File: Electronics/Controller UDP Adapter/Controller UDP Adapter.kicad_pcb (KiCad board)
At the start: 2 copper layers, 99.5 x 101 mm, 23 parts, among them J1 GNSS, J2 Pulse_J0011D01BNL, J3 Pulse_J0011D01BNL

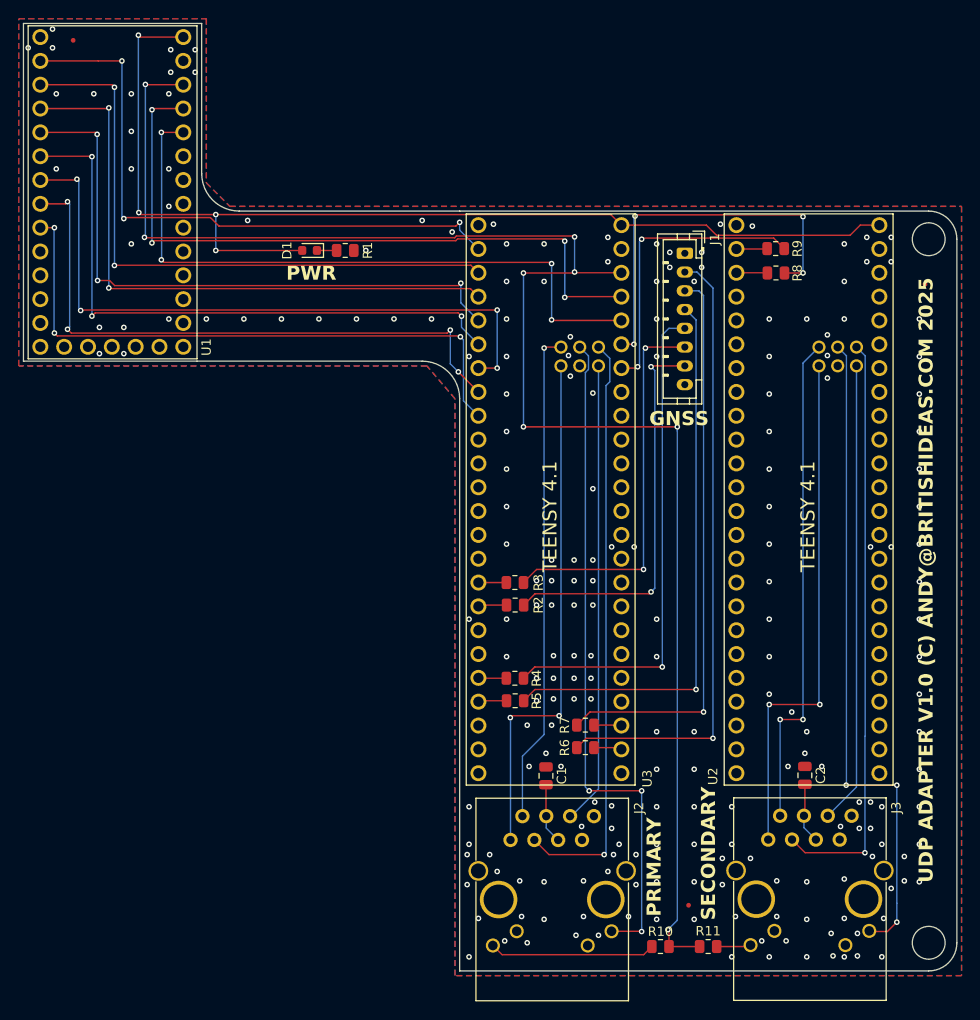
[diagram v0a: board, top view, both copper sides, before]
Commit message: Refactor, cleanup, changed PGN value size to 64 bits. Updates to base station.
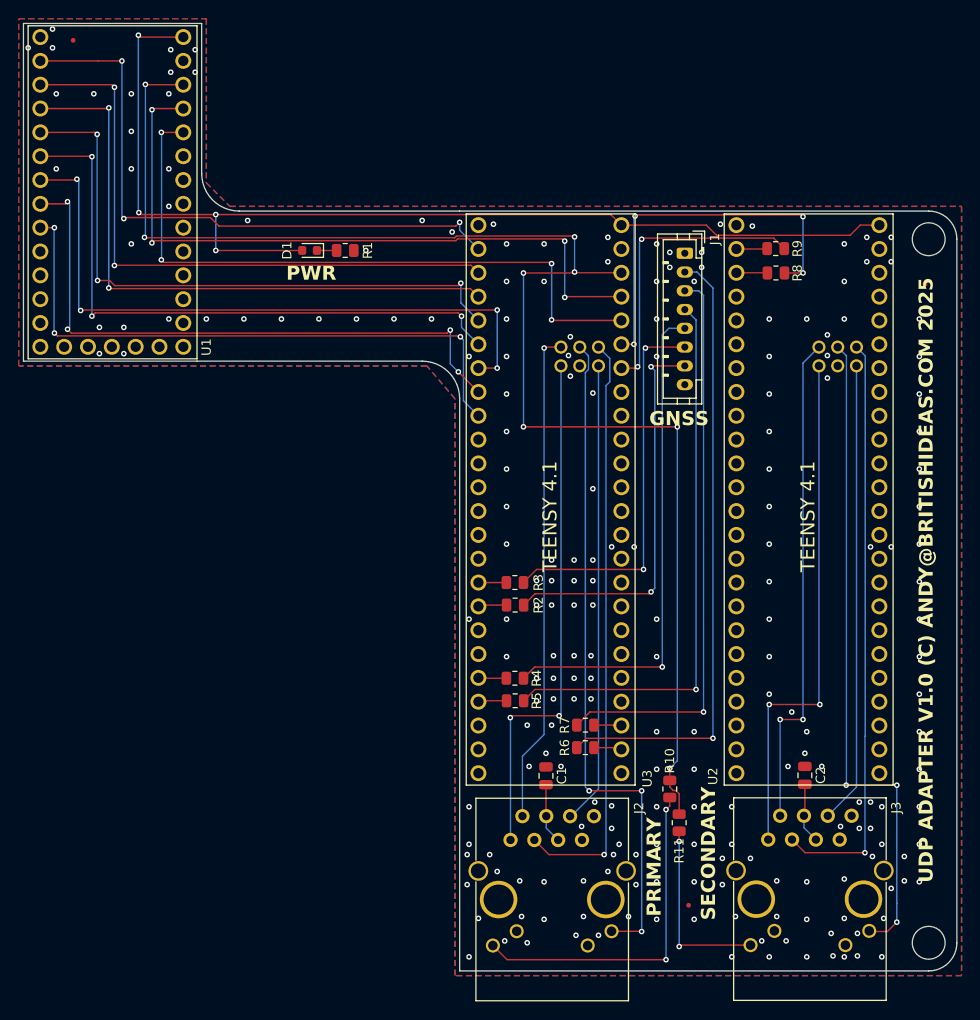
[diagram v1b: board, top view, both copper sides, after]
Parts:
- moved R10 16.8 mm to (139.4, 139.6), turned to -90 degrees
- moved R11 13.6 mm to (140.4, 143.2), turned to -90 degrees
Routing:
- net Net-(J2-Pad9): track 17.7 -> 36.5 mm, vias 0 -> 2
- net +3V3: track 172.6 -> 155.6 mm
- net Net-(J3-Pad9): track 3.67 -> 20.2 mm, vias 0 -> 2
